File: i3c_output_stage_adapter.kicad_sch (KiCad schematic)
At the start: 60 parts, among them J1 PinSocket_2x12_P2.54mm_Drill1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, J2 PinSocket_2x6_P2.54mm_Drill1.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, J3 Molex_Nano-Fit_1x2_SMD_105430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, J6 JST_XH_1x3_S3B-XH-A-LF-SN, J7 PinHeader_2x10_P1.27mm_SMD, Q1 DMC31D5UDJ, Q2 DMC31D5UDJ, Q3 DMC2400UV-7, Q4 DMC2400UV-7, U1 TPS7A0518P_SOT23-5, U2 SN74LVC1G240_SC70, U3 SN74LVC1G240_SC70

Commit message: [#68164] Update power supply, input and output connectors
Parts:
- removed J3: Molex_Nano-Fit_1x2_SMD_1054301202, antmicro-footprints:Conn_Molex_Nano-Fit_1x2_SMD_1054301202, symbol antmicroWire2BoardConnectors:Molex_Nano-Fit_1x2_SMD_1054301202
- removed J6: JST_XH_1x3_S3B-XH-A-LF-SN, antmicro-footprints:Conn_JST_XH_1x3_S3B-XH-A-LF-SN, symbol antmicroWire2BoardConnectors:JST_XH_1x3_S3B-XH-A-LF-SN
- added C5: C_10n_0402, antmicro-footprints:C_0402_1005Metric, symbol antmicroCapacitors0402:C_10n_0402
- added C6: C_100n_16V_X7R_0402, antmicro-footprints:C_0402_1005Metric, symbol antmicroCapacitors0402:C_100n_16V_X7R_0402
- added C7, C8, C9: C_1u_0603, antmicro-footprints:C_0603_1608Metric, symbol antmicroCapacitors0603:C_1u_0603
- added D3: LED_G_0402_VLMTG1500-GS08, antmicro-footprints:LED_0402_1005Metric_G, symbol antmicroLEDIndicationDiscrete:LED_G_0402_VLMTG1500-GS08
- added J3: JST_SH_1x4_SM04B-SRSS-TB-LF-SN, antmicro-footprints:Conn_JST_SH_1x4_SM04B-SRSS-TB-LF-SN, symbol antmicroWire2BoardConnectors:JST_SH_1x4_SM04B-SRSS-TB-LF-SN
- added J4: USB-C_CUI_UJC-HP-3-SMT-TR, antmicro-footprints:USB-C_Receptacle_CUI_UJC-HP-3-SMT-TR, symbol antmicroUSBConnectors:USB-C_CUI_UJC-HP-3-SMT-TR
- added J5: PinHeader_1x3_P2.54mm_Drill1.1mm, antmicro-footprints:PinHeader_1x3_P2.54mm_Drill1.1mm, symbol antmicroGenericPinHeaders:PinHeader_1x3_P2.54mm_Drill1.1mm
- added J6: PinHeader_1x3_P2.54mm_Drill1.1mm_Horizontal, antmicro-footprints:PinHeader_1x3_P2.54mm_Horizontal, symbol antmicroGenericPinHeaders:PinHeader_1x3_P2.54mm_Drill1.1mm_Horizontal
- added L1, L2: FB_120Z_2A_Murata-BLM18PG_0603, antmicro-footprints:FB_0603_1608Metric, symbol antmicroFerriteBeadsandChips:FB_120Z_2A_Murata-BLM18PG_0603
- added Q5: DMG1012T-7, antmicro-footprints:SOT-523, symbol antmicroTransistorsFETsMOSFETsSingle:DMG1012T-7
- added R26, R27: R_5k1_0402, antmicro-footprints:R_0402_1005Metric, symbol antmicroResistors0402:R_5k1_0402
- added R28: 4x0R_0402_array, antmicro-footprints:4x0R_0402_array_EXB28V, symbol antmicroResistorNetworksArrays:4x0R_0402_array
- added R29: R_2k_0402, antmicro-footprints:R_0402_1005Metric, symbol antmicroResistors0402:R_2k_0402
- added R30: R_10k_0402, antmicro-footprints:R_0402_1005Metric, symbol antmicroResistors0402:R_10k_0402
- added U4: TLV70033_SC70, antmicro-footprints:SC-70-5, symbol antmicroPMICVoltageRegulatorsLinear:TLV70033_SC70
- J2: now not fitted
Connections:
- net +1V8: now also Q5.1 (G), R30.2; no longer R17.2
- net +3V3: now also R17.2, J3.2, J5.2; no longer J2.11, J2.12
- net GND: now also C5.2, C6.2, C7.2, C8.2, C9.2, D3.1 (C), J3.1, J3.MP, J4.A12 (GND), J4.B12 (GND), J6.2, L1.2, Q5.2 (S), R26.2, R27.2, R30.1, U4.2 (GND); no longer D1.1 (C), J1.17, J1.19, J1.21, J1.23
- net SCL: now also J1.18, J2.2, J3.4, J6.1; no longer J1.24
- net SCL_DOWN: now also J1.16; no longer J1.20
- net SCL_EN/PULL: now also J1.22, J2.6; no longer J1.16
- net SCL_IN/PUSH: now also J1.20, J2.4; no longer J1.14
- net SCL_UP: now also J1.24, J2.8; no longer J1.18
- net SDA: now also J1.8, J3.3, J6.3, R28.4 (R4.1); no longer J1.22
- net SDA_DOWN: now also J1.6; no longer J1.12
- net SDA_EN/PULL: now also J1.12, R28.2 (R2.1); no longer J1.8
- net SDA_IN/PUSH: now also J1.10, R28.3 (R3.1); no longer J1.6
- net SDA_UP: now also J1.14, R28.1 (R1.1); no longer J1.10
- net PMOD1: now reaches J2.1
- net PMOD1: now also J1.17, R28.8 (R1.2)
- net PMOD3: now reaches J2.3
- net PMOD3: now also J1.19, R28.7 (R2.2)
- net PMOD5: now reaches J2.5
- net PMOD5: now also J1.21, R28.6 (R3.2)
- net PMOD7: now reaches J2.7
- net PMOD7: now also J1.23, R28.5 (R4.2)
- new net: D3.2 (A), R29.1
- new net: D1.1 (C), Q5.3 (D)
- new net: J4.A5 (CC_{1}), R26.1
- new net: C5.1, J4.A9 (VBUS), J4.B9 (VBUS), L2.2
- new net: J4.B5 (CC_{2}), R27.1
- new net +5V: C6.1, C7.1, L2.1, R29.2, U4.1 (VIN), U4.3 (EN)
- new net GNDREF: J4.SH, L1.1
- new net LDO_3V3: C8.1, C9.1, J5.1, U4.5 (VOUT)
- new net PMOD_3V3: J2.11, J2.12, J5.3
- no-connect marks 8 -> 0
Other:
- note added: "3.3V -> 1V8 LDO 200mA"
- note added: "5V -> 3.3V LDO 400mA"
- note removed: "3V3 -> 1V8"
- note removed: "LDO"
- note removed: "MOLEX NANO-FIT"
- note removed: "POWER STATUS"
- moved on the sheet: C1, C2, D1, D2, J1, R16, R17, R18, U1

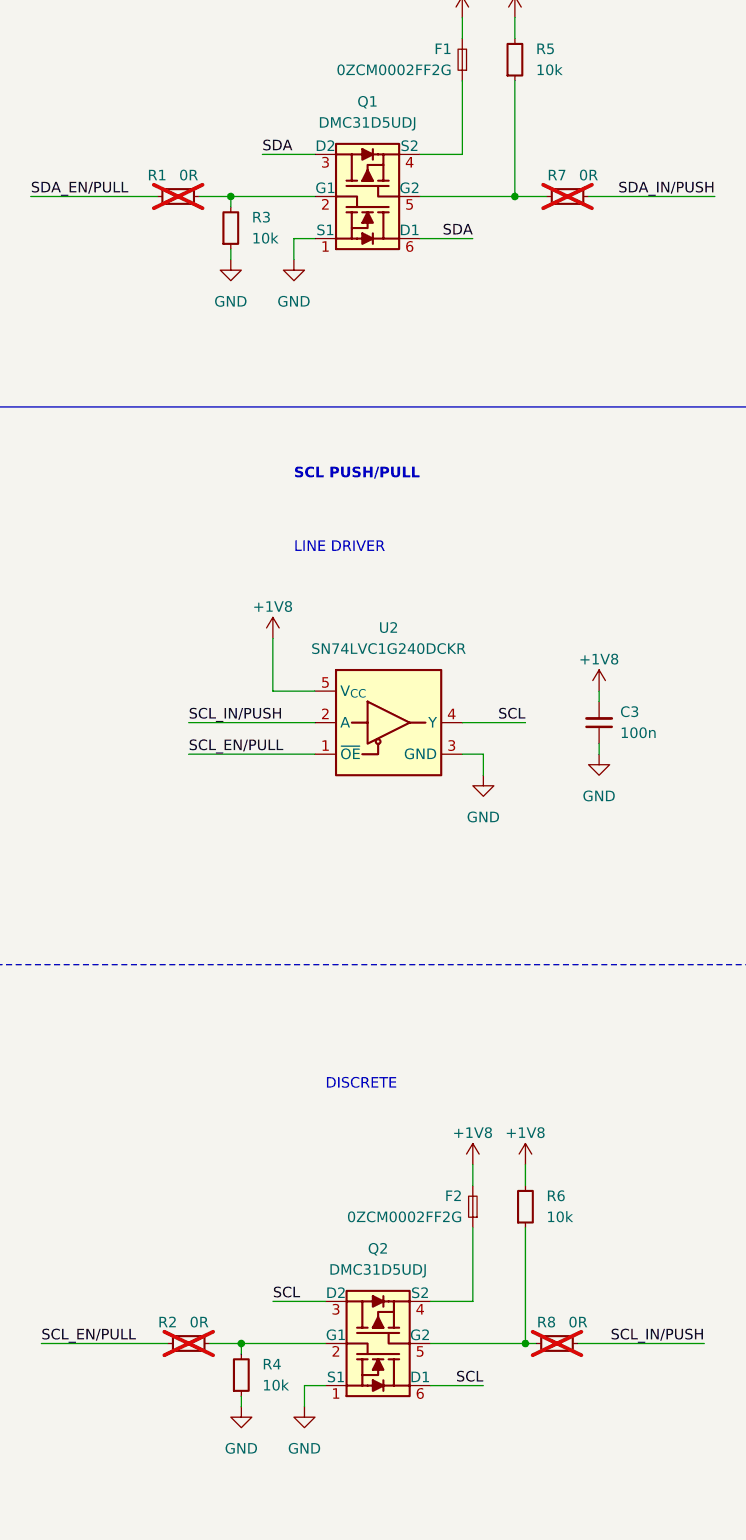
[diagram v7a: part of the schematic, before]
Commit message: [#68164] Update components, rotate PCB
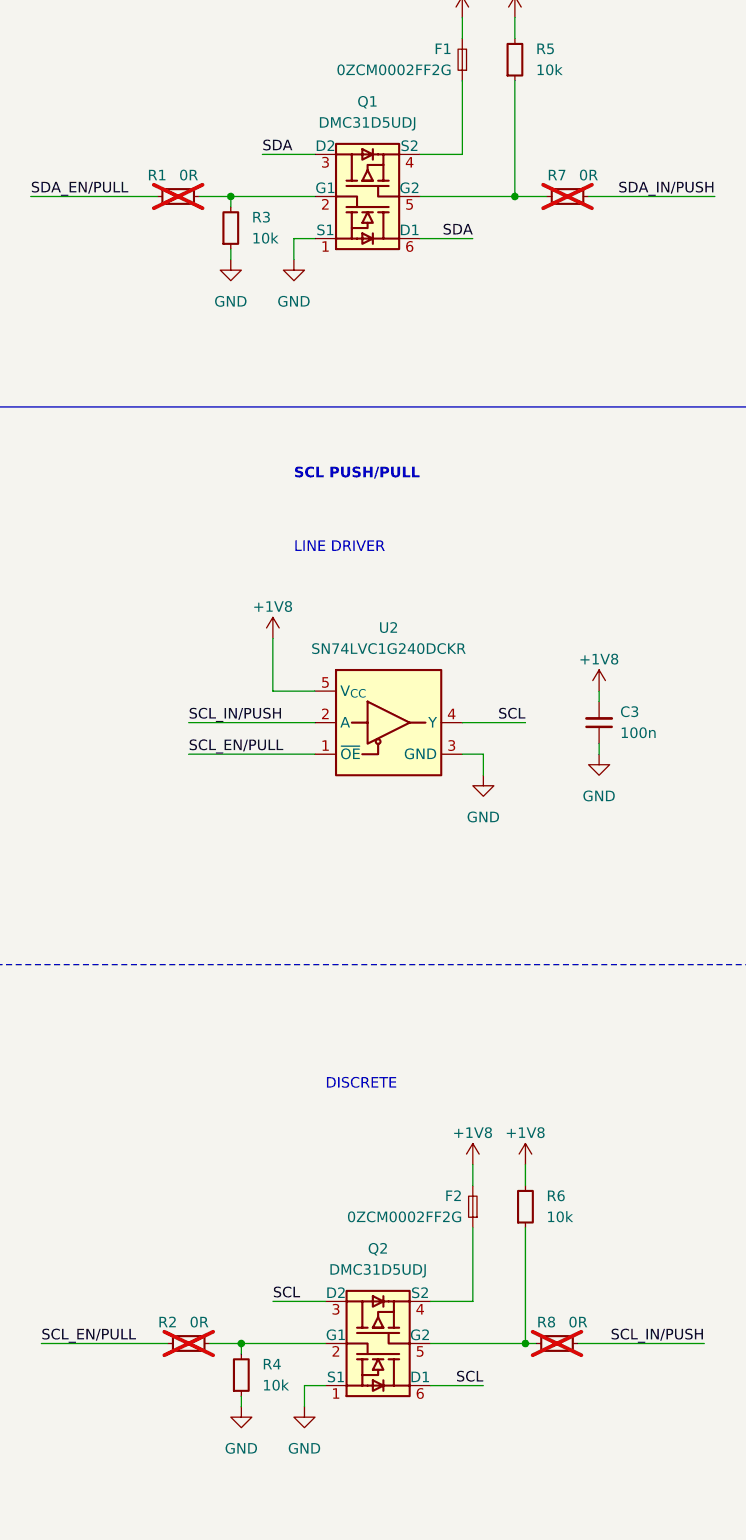
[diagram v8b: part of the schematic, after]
